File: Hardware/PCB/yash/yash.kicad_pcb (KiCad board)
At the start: 2 copper layers, 44 x 119 mm, 39 parts, among them J1 AudioJack2, J10 2_pin_Molex_header, J2 AudioJack2, J3 AudioJack2_SwitchT, J4 AudioJack2, J5 3_pin_Molex_header, J7 2_pin_Molex_header, J9 Synth_power_2x5, Q1 2N3904, U1 LF398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

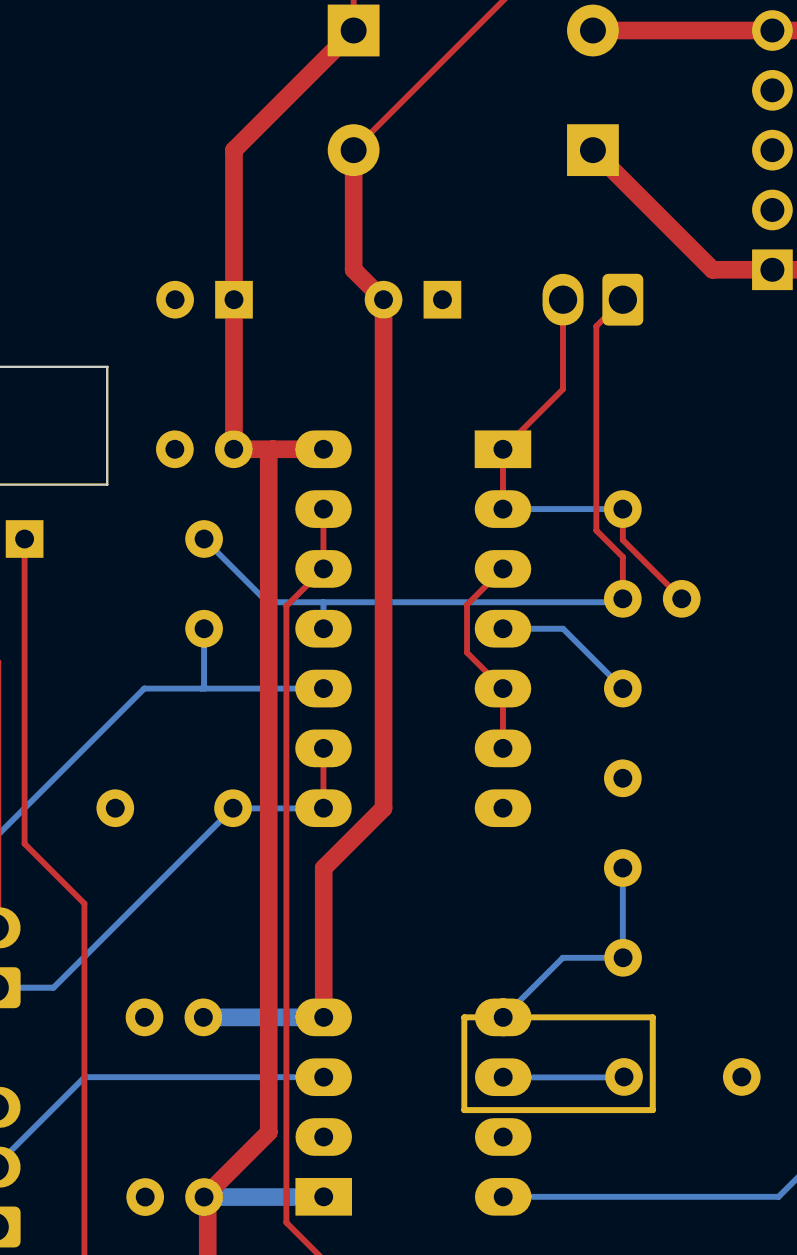
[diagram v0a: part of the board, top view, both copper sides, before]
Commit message: Redo guard ring as redundant tracks
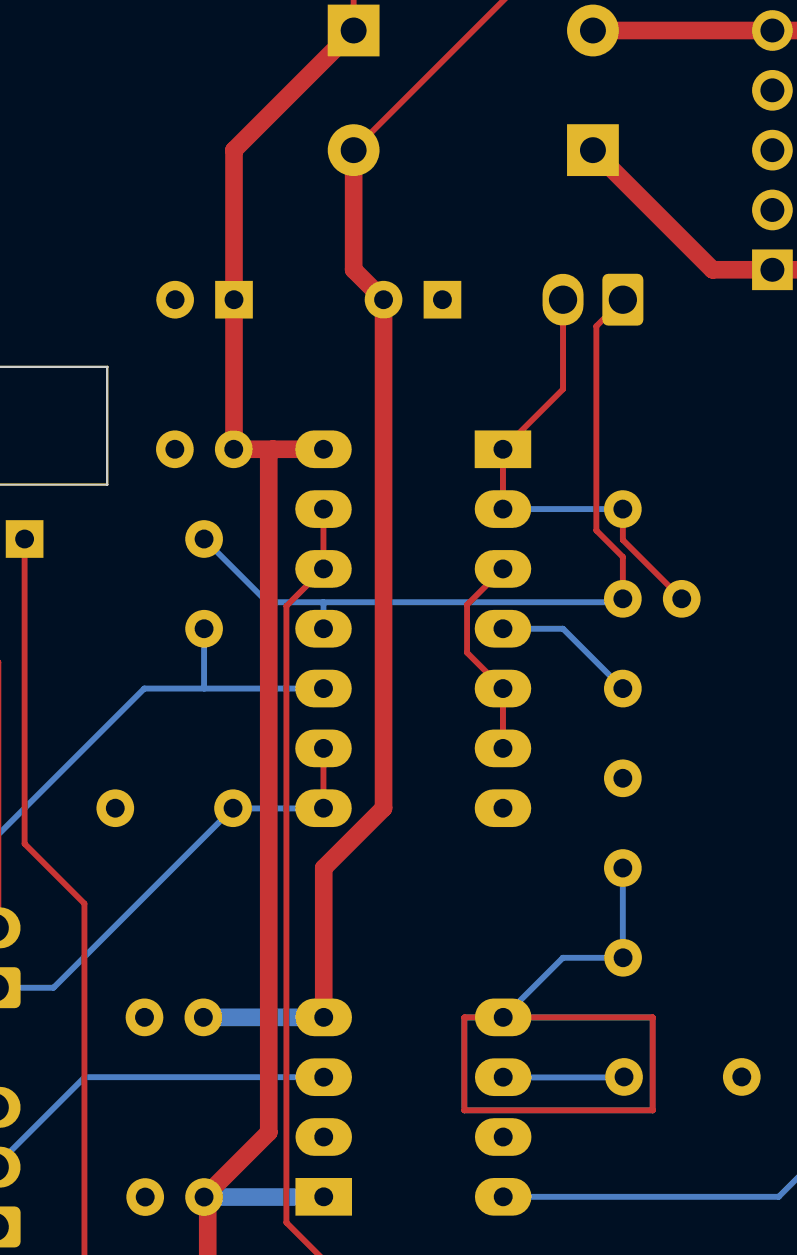
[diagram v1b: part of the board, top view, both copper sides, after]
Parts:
- U1: footprint yash:LF398_ring -> ao_tht:DIP-8_W7.62mm_Socket_LongPads
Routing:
- net /OUT398: track 9.94 -> 57.7 mm

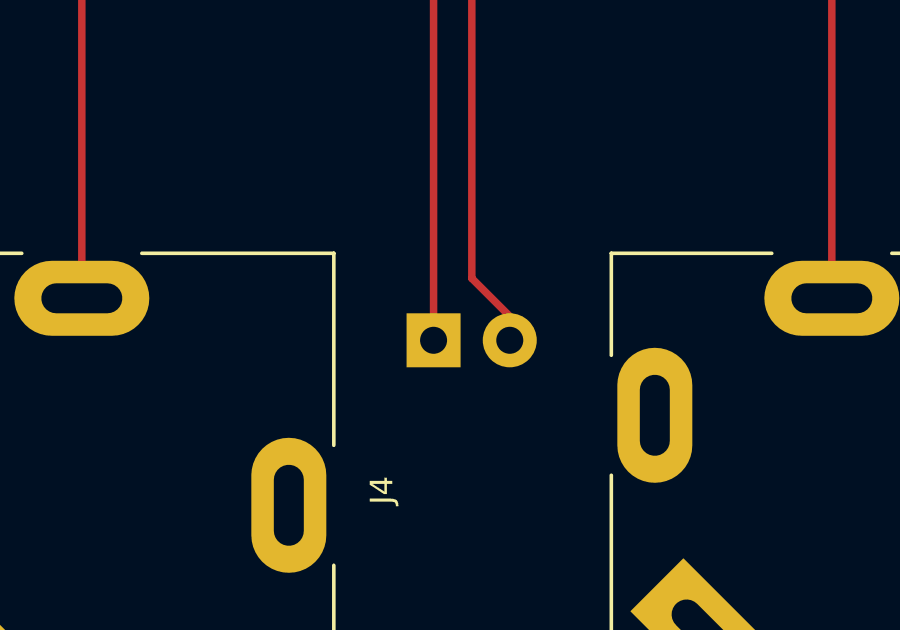
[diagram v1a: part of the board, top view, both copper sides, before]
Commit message: CW not CCW, put LED on correct side of PCB
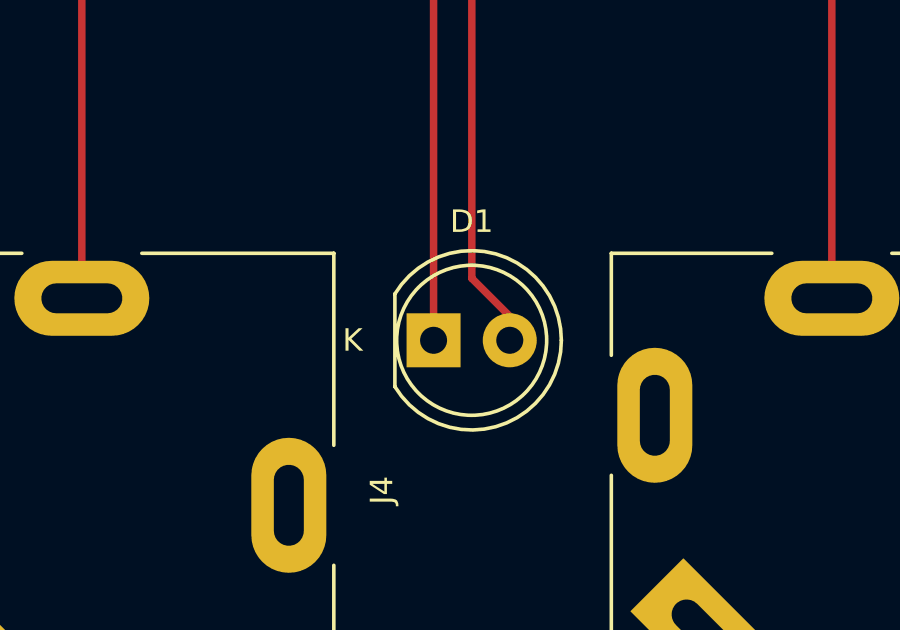
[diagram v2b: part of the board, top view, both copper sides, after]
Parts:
- D1: moved to F.Cu
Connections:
- net CLKFR_CCW renamed CLKFR_CW
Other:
- board text added: "Clock W/CW"
- board text removed: "Clock W/CCW"
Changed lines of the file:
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@@
   (net 18 "Net-(R4-Pad2)")
   (net 19 "unconnected-(U1-Pad2)")
-  (net 20 "CLKFR_CCW")
+  (net 20 "CLKFR_CW")
   (net 21 "SIGLVL_CW")
   (net 22 "SIGLVL_W")
@@
     )
   )
+  (footprint "ao_tht:LED_D5.0mm" (layer "F.Cu")
+    (at 98.725 150)
+    (descr "LED, diameter 5.0mm, 2 pins, http://cdn-reichelt.de/documents/datenblatt/A500/LL-504BC2E-009.pdf")
+    (tags "LED diameter 5.0mm 2 pins")
+    (property "SKU" "A-1553")
+    (property "Sheetfile" "yash.kicad_sch")
+    (property "Sheetname" "")
+    (property "Vendor" "Tayda")
+    (attr through_hole)
+    (fp_text reference "D1" (at 1.27 -3.96 180) (layer "F.SilkS")
+      (effects (font (size 0.75 0.75) (thickness 0.15)))
+    )
+    (fp_text value "LED_green" (at 1.27 3.96 180) (layer "F.Fab")
+      (effects (font (size 1 1) (thickness 0.15)))
+    )
+    (fp_text user "K" (at -2.7 0 180) (layer "F.SilkS")
+      (effects (font (size 0.75 0.75) (thickness 0.15)))
+    )
+    (fp_text user "${REFERENCE}" (at 1.25 0 180) (layer "F.Fab")
+      (effects (font (size 0.8 0.8) (thickness 0.2)))
+    )
+    (fp_line (start -1.29 -1.545) (end -1.29 1.545) (layer "F.SilkS") (width 0.12))
+    (fp_arc (start 4.26 -0.000462) (mid 2.072002 2.880433) (end -1.29 1.54483) (layer "F.SilkS") (width 0.12))
+    (fp_arc (start -1.29 -1.54483) (mid 2.072002 -2.880433) (end 4.26 0.000462) (layer "F.SilkS") (width 0.12))
+    (fp_circle (center 1.27 0) (end 3.77 0) (layer "F.SilkS") (width 0.12) (fill none))
+    (fp_line (start -1.95 3.25) (end 4.5 3.25) (layer "F.CrtYd") (width 0.05))
+    (fp_line (start 4.5 3.25) (end 4.5 -3.25) (layer "F.CrtYd") (width 0.05))
+    (fp_line (start -1.95 -3.25) (end -1.95 3.25) (layer "F.CrtYd") (width 0.05))
+    (fp_line (start 4.5 -3.25) (end -1.95 -3.25) (layer "F.CrtYd") (width 0.05))
+    (fp_line (start -1.23 -1.469694) (end -1.23 1.469694) (layer "F.Fab") (width 0.1))
+    (fp_arc (start -1.23 -1.469694) (mid 4.17 0.000016) (end -1.230016 1.469666) (layer "F.Fab") (width 0.1))
+    (fp_circle (center 1.27 0) (end 3.77 0) (layer "F.Fab") (width 0.1) (fill none))
+    (pad "1" thru_hole rect locked (at 0 0) (size 1.8 1.8) (drill 0.9) (layers *.Cu *.Mask)
+      (net 9 "Net-(D1-Pad1)") (pinfunction "K") (pintype "passive"))
+    (pad "2" thru_hole circle locked (at 2.54 0) (size 1.8 1.8) (drill 0.9) (layers *.Cu *.Mask)
+      (net 10 "Net-(D1-Pad2)") (pinfunction "A") (pintype "passive"))
+    (model "${KICAD_AOKICAD}/ao_tht_3d/LED_D5.0mm.wrl"
+      (offset (xyz 0 0 0))
+      (scale (xyz 1 1 1))
+      (rotate (xyz 0 0 0))
+    )
+  )
   (footprint "ao_tht:TestPoint_THTPad_1.5x1.5mm_Drill0.7mm" (layer "F.Cu")
     (at 102.54 47.37 180)
@@
     )
   )
-  (footprint "ao_tht:LED_D5.0mm" (layer "B.Cu")
-    (at 98.725 150)
-    (descr "LED, diameter 5.0mm, 2 pins, http://cdn-reichelt.de/documents/datenblatt/A500/LL-504BC2E-009.pdf")
-    (tags "LED diameter 5.0mm 2 pins")
-    (property "SKU" "A-1553")
-    (property "Sheetfile" "yash.kicad_sch")
-    (property "Sheetname" "")
-    (property "Vendor" "Tayda")
-    (attr through_hole)
-    (fp_text reference "D1" (at 1.27 3.96) (layer "B.SilkS")
-      (effects (font (size 0.75 0.75) (thickness 0.15)) (justify mirror))
-    )
-    (fp_text value "LED_green" (at 1.27 -3.96) (layer "B.Fab")
-      (effects (font (size 1 1) (thickness 0.15)) (justify mirror))
-    )
-    (fp_text user "K" (at -2.7 0) (layer "B.SilkS")
-      (effects (font (size 0.75 0.75) (thickness 0.15)) (justify mirror))
-    )
-    (fp_text user "${REFERENCE}" (at 1.25 0) (layer "B.Fab")
-      (effects (font (size 0.8 0.8) (thickness 0.2)) (justify mirror))
-    )
-    (fp_line (start -1.29 1.545) (end -1.29 -1.545) (layer "B.SilkS") (width 0.12))
-    (fp_arc (start -1.29 -1.54483) (mid 2.072002 -2.880433) (end 4.26 0.000462) (layer "B.SilkS") (width 0.12))
-    (fp_arc (start 4.26 -0.000462) (mid 2.072002 2.880433) (end -1.29 1.54483) (layer "B.SilkS") (width 0.12))
-    (fp_circle (center 1.27 0) (end 3.77 0) (layer "B.SilkS") (width 0.12) (fill none))
-    (fp_line (start -1.95 -3.25) (end 4.5 -3.25) (layer "B.CrtYd") (width 0.05))
-    (fp_line (start 4.5 -3.25) (end 4.5 3.25) (layer "B.CrtYd") (width 0.05))
-    (fp_line (start -1.95 3.25) (end -1.95 -3.25) (layer "B.CrtYd") (width 0.05))
-    (fp_line (start 4.5 3.25) (end -1.95 3.25) (layer "B.CrtYd") (width 0.05))
-    (fp_line (start -1.23 1.469694) (end -1.23 -1.469694) (layer "B.Fab") (width 0.1))
-    (fp_arc (start -1.230016 -1.469666) (mid 4.17 -0.000016) (end -1.23 1.469694) (layer "B.Fab") (width 0.1))
-    (fp_circle (center 1.27 0) (end 3.77 0) (layer "B.Fab") (width 0.1) (fill none))
-    (pad "1" thru_hole rect locked (at 0 0) (size 1.8 1.8) (drill 0.9) (layers *.Cu *.Mask)
-      (net 9 "Net-(D1-Pad1)") (pinfunction "K") (pintype "passive"))
-    (pad "2" thru_hole circle locked (at 2.54 0) (size 1.8 1.8) (drill 0.9) (layers *.Cu *.Mask)
-      (net 10 "Net-(D1-Pad2)") (pinfunction "A") (pintype "passive"))
-    (model "${KICAD_AOKICAD}/ao_tht_3d/LED_D5.0mm.wrl"
-      (offset (xyz 0 0 0))
-      (scale (xyz 1 1 1))
-      (rotate (xyz 0 0 0))
-    )
-  )
   (footprint "ao_tht:R_Axial_DIN0207_L6.3mm_D2.5mm_P10.16mm_Horizontal" (layer "B.Cu")
     (at 93.65 118.49 90)
@@
     (fp_line (start 6.1 2.25) (end -1.1 2.25) (layer "B.Fab") (width 0.1))
     (pad "1" thru_hole circle (at 0 0 180) (size 1.6 1.6) (drill 0.8) (layers *.Cu *.Mask)
-      (net 20 "CLKFR_CCW") (pintype "passive"))
+      (net 20 "CLKFR_CW") (pintype "passive"))
     (pad "2" thru_hole circle (at 5 0 180) (size 1.6 1.6) (drill 0.8) (layers *.Cu *.Mask)
       (net 1 "GND") (pintype "passive"))
@@
     (fp_line (start 3.81 2.92) (end -1.27 2.92) (layer "B.Fab") (width 0.1))
     (pad "1" thru_hole roundrect locked (at 0 0 90) (size 1.74 2.2) (drill 1.2) (layers *.Cu *.Mask) (roundrect_rratio 0.143678)
-      (net 20 "CLKFR_CCW") (pinfunction "Pin_1") (pintype "passive"))
+      (net 20 "CLKFR_CW") (pinfunction "Pin_1") (pintype "passive"))
     (pad "2" thru_hole oval locked (at 2.54 0 90) (size 1.74 2.2) (drill 1.2) (layers *.Cu *.Mask)
       (net 23 "CLKFR_W") (pinfunction "Pin_2") (pintype "passive"))
@@
       (net 1 "GND") (pinfunction "GND") (pintype "power_in"))
     (pad "8" thru_hole oval locked (at 7.62 -15.24 180) (size 2.4 1.6) (drill 0.8) (layers *.Cu *.Mask)
-      (net 20 "CLKFR_CCW") (pintype "input"))
+      (net 20 "CLKFR_CW") (pintype "input"))
     (pad "9" thru_hole oval locked (at 7.62 -12.7 180) (size 2.4 1.6) (drill 0.8) (layers *.Cu *.Mask)
-      (net 20 "CLKFR_CCW") (pintype "input"))
+      (net 20 "CLKFR_CW") (pintype "input"))
     (pad "10" thru_hole oval locked (at 7.62 -10.16 180) (size 2.4 1.6) (drill 0.8) (layers *.Cu *.Mask)
       (net 14 "Net-(J3-PadTN)") (pintype "output"))
@@
     (effects (font (size 1.5 1.5) (thickness 0.3)) (justify mirror))
   )
-  (gr_text "Clock W/CCW" (at 86.792 92.963 90) (layer "B.SilkS")
+  (gr_text "Clock W/CW" (at 86.792 92.963 90) (layer "B.SilkS")
     (effects (font (size 0.75 0.75) (thickness 0.15)) (justify mirror))
   )
